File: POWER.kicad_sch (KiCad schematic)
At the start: 44 parts, among them U4 LMR43620R5RPER, U5 LMR604303SRAKRQ1, U6 AP7361C-33FGE-7, U7 AP7361C-33FGE-7

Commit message: update name
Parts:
- removed C17, C19, C23: 100n, Capacitor_SMD:C_0402_1005Metric, symbol Device:C_Small
- removed R10, R17, R18: 10K, Resistor_SMD:R_0402_1005Metric, symbol Device:R_Small
- removed R11, R14: 1K, Resistor_SMD:R_0402_1005Metric, symbol Device:R_Small
- removed R13: 20K, Resistor_SMD:R_0402_1005Metric, symbol Device:R_Small
- removed TP1, TP2: TestPoint, symbol Connector:TestPoint
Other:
- note removed: "POWER"
- company: Pierluigi Colangeli, PhD -> (none)
- title: LEVIA H7 -> (none)

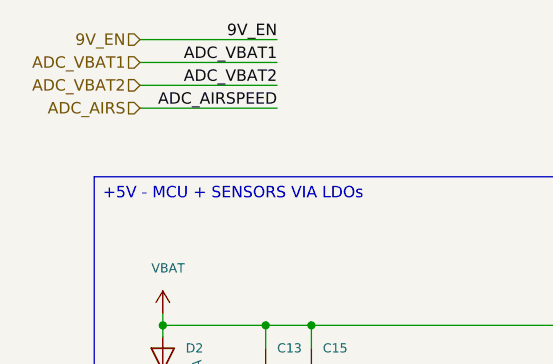
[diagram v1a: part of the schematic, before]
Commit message: upsadte SPI4 set to Baro
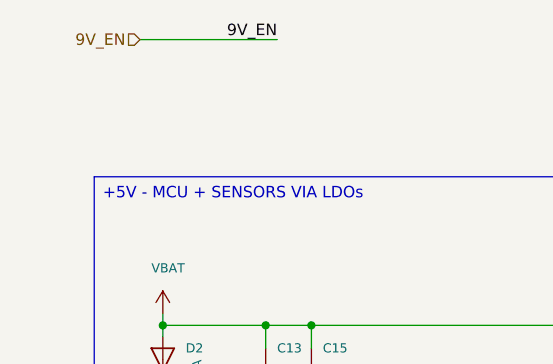
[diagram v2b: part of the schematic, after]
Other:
- title: (none) -> H743_ARDUPILOT
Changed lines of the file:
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@@
 	(generator "eeschema")
 	(generator_version "10.0")
-	(paper "A4")
+	(paper "A3")
 	(title_block
+		(title "H743_ARDUPILOT")
 		(date "2026-09-24")
 	)
@@
 	(wire
 		(pts
-			(xy 27.94 36.83) (xy 43.18 36.83)
-		)
-		(stroke
-			(width 0)
-			(type default)
-		)
-	)
-	(wire
-		(pts
 			(xy 46.99 68.58) (xy 46.99 71.12)
 		)
@@
 	(wire
 		(pts
-			(xy 27.94 31.75) (xy 43.18 31.75)
-		)
-		(stroke
-			(width 0)
-			(type default)
-		)
-	)
-	(wire
-		(pts
 			(xy 148.59 116.84) (xy 153.67 116.84)
 		)
@@
 		(pts
 			(xy 146.05 68.58) (xy 146.05 71.12)
-		)
-		(stroke
-			(width 0)
-			(type default)
-		)
-	)
-	(wire
-		(pts
-			(xy 27.94 34.29) (xy 43.18 34.29)
 		)
 		(stroke
@@
 		)
 	)
-	(label "ADC_VBAT1"
-		(at 43.18 31.75 180)
-		(effects
-			(font
-				(size 1.27 1.27)
-			)
-			(justify right bottom)
-		)
-	)
 	(label "9V_EN"
 		(at 53.34 119.38 0)
@@
 		)
 	)
-	(label "ADC_AIRSPEED"
-		(at 43.18 36.83 180)
-		(effects
-			(font
-				(size 1.27 1.27)
-			)
-			(justify right bottom)
-		)
-	)
 	(label "SW_5V"
 		(at 109.22 64.77 0)
@@
 		)
 	)
-	(label "ADC_VBAT2"
-		(at 43.18 34.29 180)
-		(effects
-			(font
-				(size 1.27 1.27)
-			)
-			(justify right bottom)
-		)
-	)
 	(hierarchical_label "9V_EN"
 		(shape input)
@@
 		(effects
 			(font
-				(size 1.27 1.27)
-			)
-			(justify right)
-		)
-	)
-	(hierarchical_label "ADC_AIRS"
-		(shape input)
-		(at 27.94 36.83 180)
-		(effects
-			(font
-				(size 1.27 1.27)
-			)
-			(justify right)
-		)
-	)
-	(hierarchical_label "ADC_VBAT2"
-		(shape input)
-		(at 27.94 34.29 180)
-		(effects
-			(font
-				(size 1.27 1.27)
-			)
-			(justify right)
-		)
-	)
-	(hierarchical_label "ADC_VBAT1"
-		(shape input)
-		(at 27.94 31.75 180)
-		(effects
-			(font

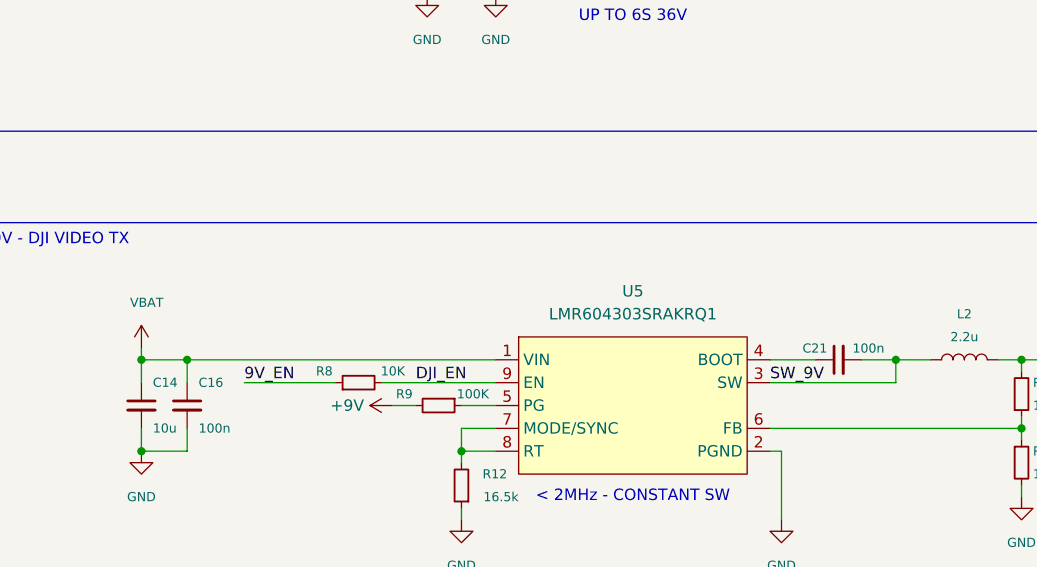
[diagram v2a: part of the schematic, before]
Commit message: remove 9v_EN 9v power supply alwaye activated
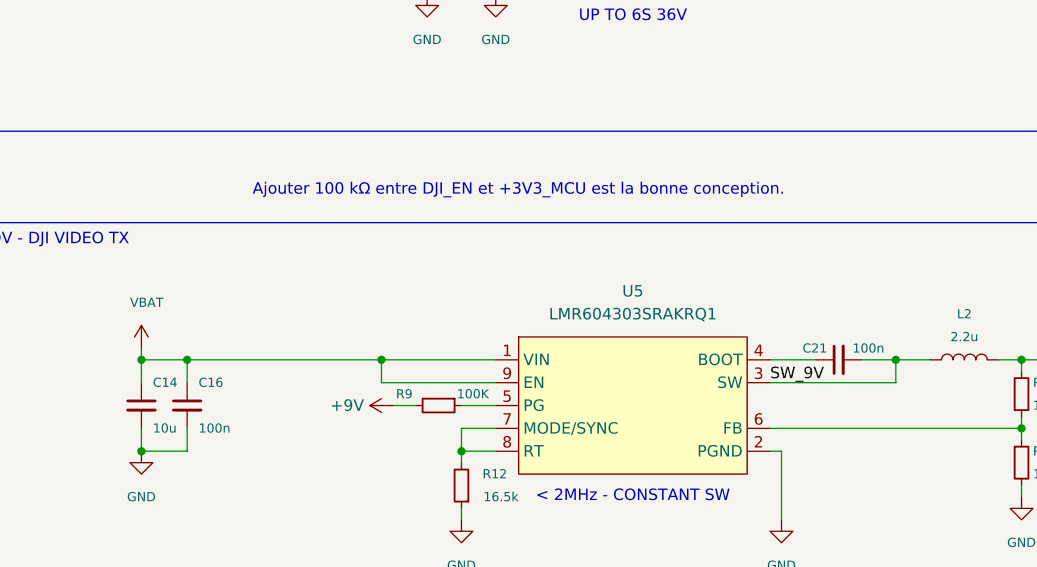
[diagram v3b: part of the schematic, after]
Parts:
- removed R8: 10K, Resistor_SMD:R_0402_1005Metric, symbol Device:R_Small
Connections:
- net DJI_EN is gone; now on net VBAT: U5.9 (EN)
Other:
- note added: "Ajouter 100 kΩ entre DJI_EN et +3V3_MCU est la bonne conception."
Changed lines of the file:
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@@
 		)
 	)
+	(text "Ajouter 100 kΩ entre DJI_EN et +3V3_MCU est la bonne conception."
+		(exclude_from_sim no)
+		(at 83.82 98.044 0)
+		(effects
+			(font
+				(size 1.27 1.27)
+			)
+		)
+	)
 	(text_box "+3V3 - MCU"
 		(exclude_from_sim no)
@@
 	)
 	(junction
+		(at 68.58 116.84)
+		(diameter 0)
+		(color 0 0 0 0)
+	)
+	(junction
 		(at 158.75 116.84)
 		(diameter 0)
@@
 	(wire
 		(pts
-			(xy 53.34 119.38) (xy 63.5 119.38)
-		)
-		(stroke
-			(width 0)
-			(type default)
-		)
-	)
-	(wire
-		(pts
 			(xy 205.74 116.84) (xy 205.74 118.11)
 		)
@@
 	(wire
 		(pts
+			(xy 68.58 116.84) (xy 81.28 116.84)
+		)
+		(stroke
+			(width 0)
+			(type default)
+		)
+	)
+	(wire
+		(pts
 			(xy 69.85 121.92) (xy 72.39 121.92)
 		)
@@
 	(wire
 		(pts
-			(xy 46.99 116.84) (xy 81.28 116.84)
+			(xy 46.99 116.84) (xy 68.58 116.84)
 		)
 		(stroke
@@
 	(wire
 		(pts
+			(xy 68.58 116.84) (xy 68.58 119.38)
+		)
+		(stroke
+			(width 0)
+			(type default)
+		)
+	)
+	(wire
+		(pts
 			(xy 139.7 124.46) (xy 139.7 125.73)
 		)
@@
 		)
 	)
-	(label "DJI_EN"
-		(at 72.39 119.38 0)
-		(effects
-			(font
-				(size 1.27 1.27)
-			)
-			(justify left bottom)
-		)
-	)
 	(label "SW_9V"
 		(at 111.76 119.38 0)
@@
 		)
 	)
-	(label "9V_EN"
-		(at 53.34 119.38 0)
-		(effects
-			(font
-				(size 1.27 1.27)
-			)
-			(justify left bottom)
-		)
-	)
 	(label "SW_5V"
 		(at 109.22 64.77 0)
@@
 					(unit 1)
 				)
-			)
-		)
-	)
-	(symbol
-		(lib_id "Device:R_Small")
-		(at 66.04 119.38 90)
-		(unit 1)
-		(body_style 1)
-		(exclude_from_sim no)
-		(in_bom yes)
-		(on_board yes)
-		(in_pos_files yes)
-		(dnp no)
-		(property "Reference" "R8"
-			(at 62.23 118.11 90)
-			(show_name no)
-			(do_not_autoplace no)
-			(effects
-				(font
-					(size 1.016 1.016)
-				)
-			)
-		)
-		(property "Value" "10K"
-			(at 69.85 118.11 90)
-			(show_name no)
-			(do_not_autoplace no)
-			(effects
-				(font
-					(size 1.016 1.016)
-				)
-			)
-		)
-		(property "Footprint" "Resistor_SMD:R_0402_1005Metric"
-			(at 66.04 119.38 0)
-			(hide yes)
-			(show_name no)
-			(do_not_autoplace no)
-			(effects
-				(font
-					(size 1.27 1.27)
-				)
-			)
-		)
-		(property "Datasheet" ""
-			(at 66.04 119.38 0)
-			(hide yes)
-			(show_name no)
-			(do_not_autoplace no)
-			(effects
-				(font
-					(size 1.27 1.27)
-				)
-			)
-		)
-		(property "Description" "Resistor, small symbol"
-			(at 66.04 119.38 0)
-			(hide yes)
-			(show_name no)
-			(do_not_autoplace no)
-			(effects
-				(font
-					(size 1.27 1.27)
-				)
-			)
-		)
-		(property "LCSC Part" "C25744"
-			(at 66.04 119.38 90)
-			(hide yes)
-			(show_name no)
-			(do_not_autoplace no)
-			(effects
-				(font
-					(size 1.27 1.27)
-				)
-			)
-		)
-		(property "LCSC" "C25744"
-			(at 66.04 119.38 90)
-			(hide yes)
-			(show_name no)
-			(do_not_autoplace no)
-			(effects
-				(font
-					(size 1.27 1.27)
-				)
-			)
-		)
-		(property "MPN" "0402WGF1002TCE"
-			(at 66.04 119.38 90)
-			(hide yes)
-			(show_name no)
-			(do_not_autoplace no)
-			(effects
-				(font
-					(size 1.27 1.27)
-				)
-			)
-		)
-		(property "Manufacturer" "UNI-ROYAL(Uniroyal Elec)"
-			(at 66.04 119.38 90)
-			(hide yes)
-			(show_name no)
-			(do_not_autoplace no)
-			(effects
-				(font
-					(size 1.27 1.27)
-				)
-			)
-		)
-		(pin "2"
-		)
-		(pin "1"
-		)
-		(instances
-			(project "H743_Ardupilot"
-				(path "/6b768b36-fce6-4be0-9021-6d41bddc3a70/4618509d-46d5-4b32-bd9a-2bec826ec7e9"
-					(reference "R8")
-					(unit 1)
-				)

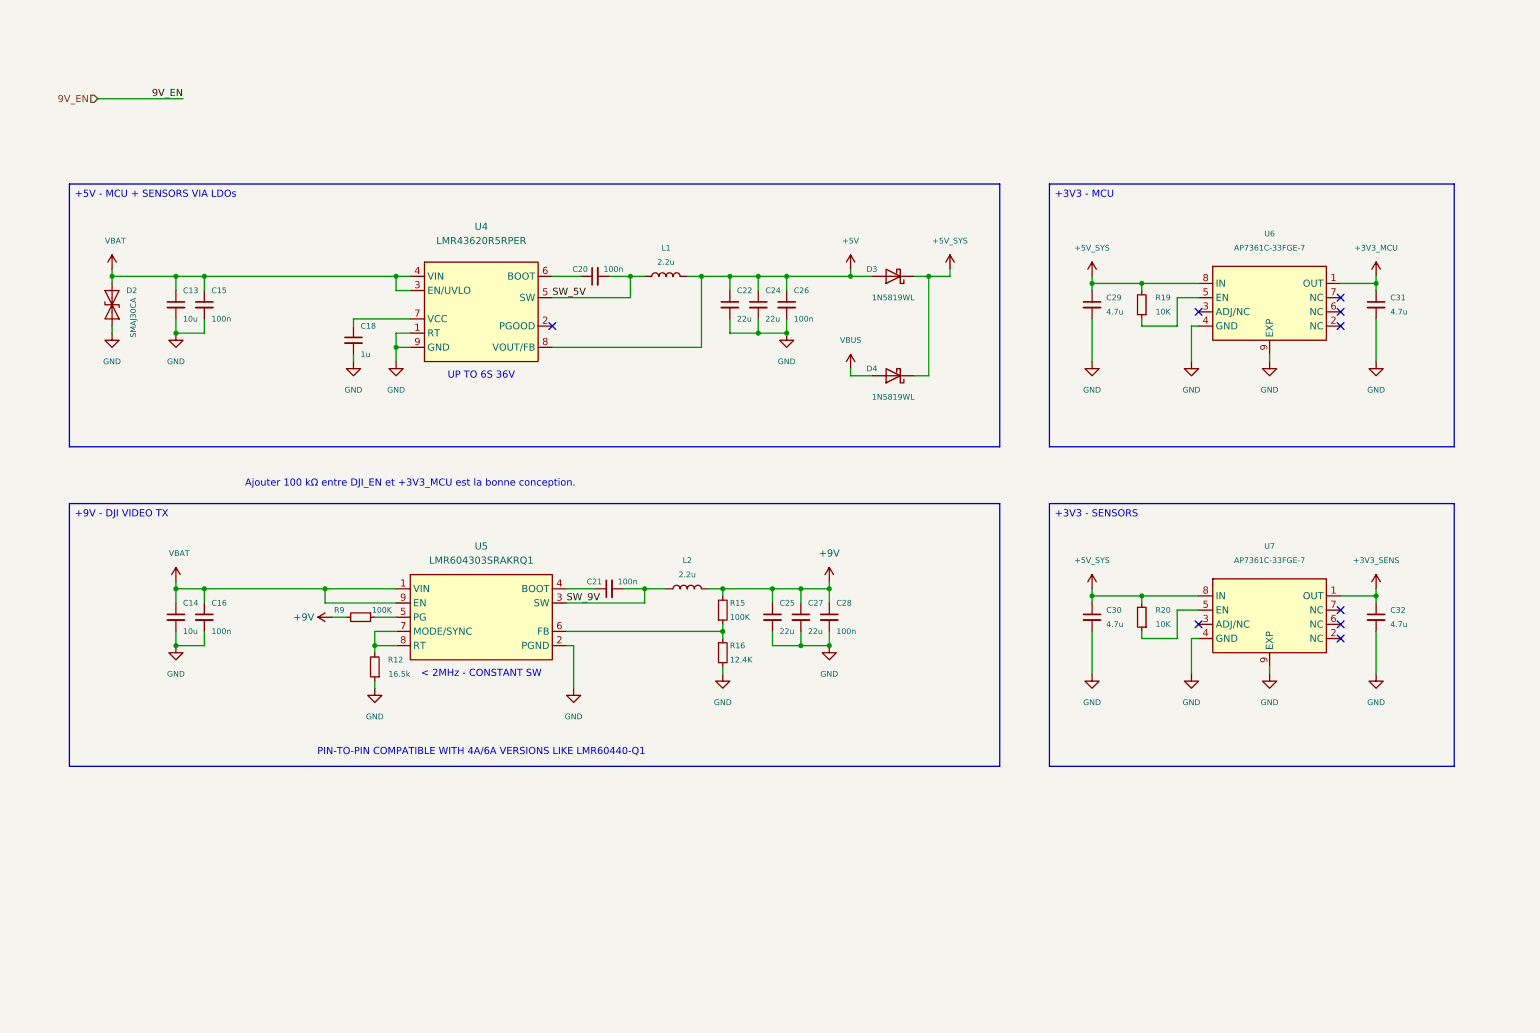
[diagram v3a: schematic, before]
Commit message: solved issue on SPI1
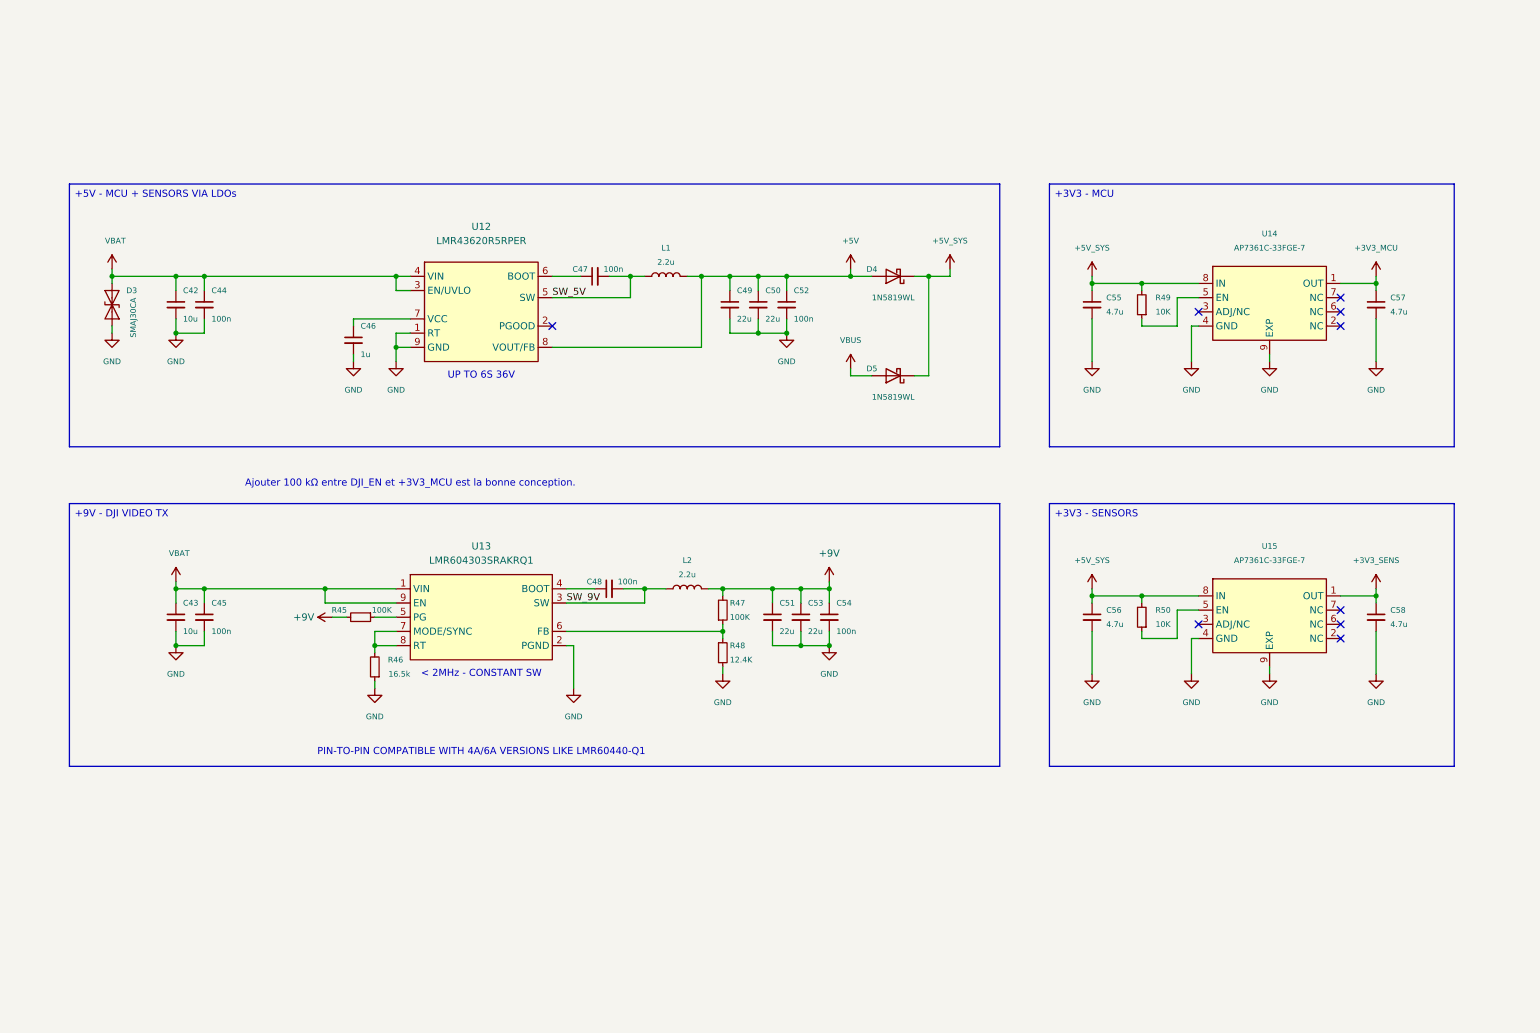
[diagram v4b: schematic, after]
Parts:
- renumbered C13 to C42, C14 to C43, C15 to C44, C16 to C45, C18 to C46, C20 to C47, C21 to C48, C22 to C49, C24 to C50, C25 to C51, C26 to C52, C27 to C53, C28 to C54, C29 to C55, C30 to C56, C31 to C57, C32 to C58, D2 to D3, D3 to D4, D4 to D5, R9 to R45, R12 to R46, R15 to R47, R16 to R48, R19 to R49, R20 to R50, U4 to U12, U5 to U13, U6 to U14, U7 to U15

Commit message: audit DigiKey metadata: POWER
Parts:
- C42, C43: DigiKey Part Number (none) -> 490-18663-1-ND; DigiKey Price Qty (none) -> 1 CT; DigiKey Specs (none) -> 10 µF ±10%, 50 V, X5R, 0805; DigiKey Status (none) -> Active; DigiKey URL (none) -> https://www.digikey.fr/fr/products/detail/murata-electronic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; DigiKey Unit Price EUR (none) -> 0.28; Footprint Audit (none) -> OK; LCSC C440198 -> (none); LCSC Part C440198 -> (none); Library Audit (none) -> KiCad standard; Package (none) -> 0805 (2012); Price Checked (none) -> 2026-09-25
- C44, C45: DigiKey Part Number (none) -> 490-10672-1-ND; DigiKey Specs (none) -> 100 nF ±10%, 50 V, X7R, 0402 (1005); DigiKey Status (none) -> Active; 50 V selected for power-domain margin; DigiKey URL (none) -> https://www.digikey.fr/fr/products/detail/murata-electronic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; Footprint Audit (none) -> OK; LCSC C307331 -> (none); LCSC Part C307331 -> (none); Library Audit (none) -> KiCad standard; MPN GRM022R60J104KE15D -> GCM155R71H104KE02D; Package (none) -> 0402 (1005 Metric); Price Checked (none) -> 2026-09-25
- C46: DigiKey Part Number (none) -> 1276-1860-1-ND; DigiKey Price Qty (none) -> 1 CT; DigiKey Specs (none) -> 1 µF ±10%, 50 V, X5R, 0603; DigiKey Status (none) -> Active; DigiKey URL (none) -> https://www.digikey.fr/en/products/detail/samsung-electro-m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; DigiKey Unit Price EUR (none) -> 0.12; Footprint Audit (none) -> OK; LCSC C15849 -> (none); LCSC Part C15849 -> (none); Library Audit (none) -> KiCad standard; Package (none) -> 0603 (1608); Price Checked (none) -> 2026-09-25
- C47, C48, C52, C54: DigiKey Part Number (none) -> 490-10672-1-ND; DigiKey Specs (none) -> 100 nF ±10%, 50 V, X7R, 0402 (1005); DigiKey Status (none) -> Active; 50 V selected for power-domain margin; DigiKey URL (none) -> https://www.digikey.fr/fr/products/detail/murata-electronic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; Footprint Audit (none) -> OK; LCSC C1525 -> (none); LCSC Part C1525 -> (none); Library Audit (none) -> KiCad standard; MPN GRM022R60J104KE15D -> GCM155R71H104KE02D; Package (none) -> 0402 (1005 Metric); Price Checked (none) -> 2026-09-25
- C49, C50, C51, C53: DigiKey Part Number (none) -> 1276-CL21A226MAYNNNECT-ND; DigiKey Price Qty (none) -> 1 CT; DigiKey Specs (none) -> 22 µF ±20%, 25 V, X5R, 0805; DigiKey Status (none) -> Active; DigiKey URL (none) -> https://www.digikey.fr/en/products/detail/samsung-electro-m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; DigiKey Unit Price EUR (none) -> 0.27; Footprint Audit (none) -> OK copper land class; verify height clearance; LCSC C45783 -> (none); LCSC Part C45783 -> (none); Library Audit (none) -> KiCad standard; MPN CL21A226MAQNNNE -> CL21A226MAYNNNE; Package (none) -> 0805 (2012), max H 1.45 mm; Price Checked (none) -> 2026-09-25
- C55, C56, C57, C58: DigiKey Part Number (none) -> 1276-1784-1-ND; DigiKey Price Qty (none) -> 1 CT; DigiKey Specs (none) -> 4.7 µF ±10%, 16 V, X5R, 0603; DigiKey Status (none) -> Active; DigiKey URL (none) -> https://www.digikey.fr/en/products/detail/samsung-electro-m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; DigiKey Unit Price EUR (none) -> 0.12; Footprint Audit (none) -> OK; LCSC C19666 -> (none); LCSC Part C19666 -> (none); Library Audit (none) -> KiCad standard; Package (none) -> 0603 (1608); Price Checked (none) -> 2026-09-25
- D3: DigiKey Price Qty (none) -> 1 CT; DigiKey Specs (none) -> Bidirectional TVS, 30 V standoff, 33.3 V breakdown min, 48.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; DigiKey Status (none) -> Active; DigiKey URL (none) -> https://www.digikey.fr/en/products/detail/diodes-incorporat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; DigiKey Unit Price EUR (none) -> 0.51; Footprint Audit (none) -> OK; Library Audit (none) -> KiCad standard; Package (none) -> DO-214AC / SMA; Price Checked (none) -> 2026-09-25
- D4, D5: value 1N5819WL -> 1N5819HW-7-F; DigiKey Part Number (none) -> 1N5819HW-FDICT-ND; DigiKey Price Qty (none) -> 1 CT; DigiKey Specs (none) -> Schottky, 40 V, 1 A, SOD-123; DigiKey Status (none) -> Active; DigiKey URL (none) -> https://www.digikey.fr/fr/products/detail/diodes-incorporat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; DigiKey Unit Price EUR (none) -> 0.27; Footprint Audit (none) -> OK; LCSC C2905650 -> (none); LCSC Part C2905650 -> (none); Library Audit (none) -> KiCad standard; MPN 1N5819W -> 1N5819HW-7-F; Manufacturer TECH PUBLIC -> Diodes Incorporated; Package (none) -> SOD-123; Price Checked (none) -> 2026-09-25
- L1, L2: DigiKey Specs (none) -> 2.2 µH, ±20%, Irms 8.9 A, Isat 6.2 A typ listing, DCR 21.5 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; DigiKey Status (none) -> Active; price not confirmed; DigiKey URL (none) -> https://www.digikey.fr/en/products/result?keywords=XGL4020-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; Footprint Audit (none) -> CHECK: current footprint is XAL4030-family; exact XGL4020 p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; Library Audit (none) -> KiCad standard footprint reused; Package (none) -> XGL4020, 4x4x2.1 mm; Price Checked (none) -> 2026-09-25
- R45, R47: DigiKey Price Qty (none) -> 1 CT; DigiKey Specs (none) -> 100K ±1%, 0402 (1005), thick film; DigiKey Status (none) -> Active / DigiKey family verified; DigiKey URL (none) -> https://www.digikey.fr/en/products/result?keywords=RC0402FR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; DigiKey Unit Price EUR (none) -> 0.09; Footprint Audit (none) -> OK; LCSC C25741 -> (none); LCSC Part C25741 -> (none); Library Audit (none) -> KiCad standard; MPN 0402WGF1003TCE -> RC0402FR-07100KL; Manufacturer UNI-ROYAL(Uniroyal Elec) -> YAGEO; Package (none) -> 0402 (1005 Metric); Price Checked (none) -> 2026-09-25
- R46: DigiKey Price Qty (none) -> 1 CT; DigiKey Specs (none) -> 16.5k ±1%, 0402 (1005), thick film; DigiKey Status (none) -> Active / DigiKey family verified; DigiKey URL (none) -> https://www.digikey.fr/en/products/result?keywords=RC0402FR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; DigiKey Unit Price EUR (none) -> 0.09; Footprint Audit (none) -> OK; LCSC C25857 -> (none); LCSC Part C25857 -> (none); Library Audit (none) -> KiCad standard; MPN 0402WGF1652TCE -> RC0402FR-0716K5L; Manufacturer UNI-ROYAL(Uniroyal Elec) -> YAGEO; Package (none) -> 0402 (1005 Metric); Price Checked (none) -> 2026-09-25
- R48: DigiKey Specs (none) -> 12.4K ±1%, 0402 (1005), thick film; DigiKey Status (none) -> Active / DigiKey family verified; DigiKey URL (none) -> https://www.digikey.fr/en/products/result?keywords=RC0402FR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; Footprint Audit (none) -> OK; LCSC C11692 -> (none); LCSC Part C11692 -> (none); Library Audit (none) -> KiCad standard; MPN 0402WGF1242TCE -> RC0402FR-0712K4L; Manufacturer UNI-ROYAL(Uniroyal Elec) -> YAGEO; Package (none) -> 0402 (1005 Metric); Price Checked (none) -> 2026-09-25
- R49, R50: DigiKey Price Qty (none) -> 1 CT; DigiKey Specs (none) -> 10K ±1%, 0402 (1005), thick film; DigiKey Status (none) -> Active / DigiKey family verified; DigiKey URL (none) -> https://www.digikey.fr/en/products/result?keywords=RC0402FR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; DigiKey Unit Price EUR (none) -> 0.09; Footprint Audit (none) -> OK; LCSC C25744 -> (none); LCSC Part C25744 -> (none); Library Audit (none) -> KiCad standard; MPN 0402WGF1002TCE -> RC0402FR-0710KL; Manufacturer UNI-ROYAL(Uniroyal Elec) -> YAGEO; Package (none) -> 0402 (1005 Metric); Price Checked (none) -> 2026-09-25
- U12: DigiKey Part Number (none) -> 296-LMR43620R5RPERCT-ND; DigiKey Price Qty (none) -> 1 CT; DigiKey Specs (none) -> 3–36 V synchronous buck, 2 A, 9-VQFN-HR 2x2 mm; DigiKey Status (none) -> Active; DigiKey URL (none) -> https://www.digikey.fr/en/products/detail/texas-instruments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; DigiKey Unit Price EUR (none) -> 1.94; Footprint Audit (none) -> CHECK: current EasyEDA footprint named 2.1x2.1; compare to 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; Library Audit (none) -> EasyEDA external; Manufacturer TI(德州仪器) -> Texas Instruments; Package (none) -> 9-VQFN-HR 2x2 mm; Price Checked (none) -> 2026-09-25
- U13: DigiKey Part Number (none) -> 296-LMR604303SRAKRQ1CT-ND; DigiKey Price Qty (none) -> 1 CT; DigiKey Specs (none) -> 3–36 V automotive synchronous buck, 3 A, 9-WQFN-HR 2.5x2 mm; DigiKey Status (none) -> Active / AEC-Q100; DigiKey URL (none) -> https://www.digikey.fr/en/products/detail/texas-instruments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; DigiKey Unit Price EUR (none) -> 2.20; Footprint Audit (none) -> OK by package name/dimensions; final overlay recommended; Library Audit (none) -> EasyEDA external; Manufacturer TI(德州仪器) -> Texas Instruments; Package (none) -> 9-WQFN-HR 2.5x2.0 mm; Price Checked (none) -> 2026-09-25
- U14, U15: DigiKey Part Number (none) -> AP7361C-33FGE-7DICT-ND; DigiKey Price Qty (none) -> 1 CT; DigiKey Specs (none) -> 3.3 V fixed LDO, 1 A, Vin max 6 V, U-DFN3030-8 Type E; DigiKey Status (none) -> Active; DigiKey URL (none) -> https://www.digikey.fr/fr/products/detail/diodes-incorporat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; DigiKey Unit Price EUR (none) -> 0.49; Footprint Audit (none) -> OK; Library Audit (none) -> EasyEDA external; Manufacturer DIODES(美台) -> Diodes Incorporated; Package (none) -> U-DFN3030-8 Type E EP; Price Checked (none) -> 2026-09-25
